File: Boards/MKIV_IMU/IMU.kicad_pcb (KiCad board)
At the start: 2 copper layers, 50.8 x 55.9 mm, 55 parts, among them J1 UF_8_RA, J4 CONN_02X03, Q1 SSM3K333R, Q2 SSM3K333R, U1 CAN_Transceiver, U2 TPS561201, U3 TCR2EF33LM, U4 BMI088, U5 ATMEGA16M1, Y1 Crystal_SMD

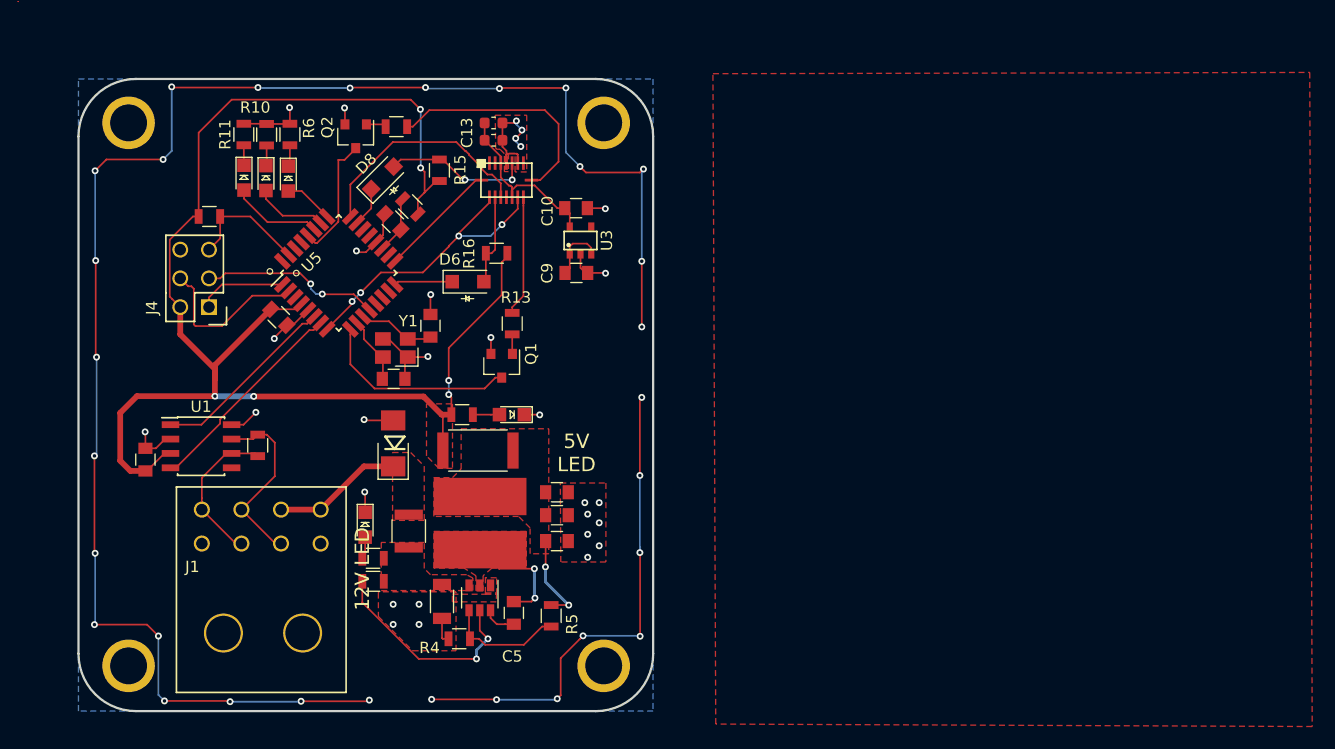
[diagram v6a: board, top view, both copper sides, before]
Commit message: updated fets for layout for new net list
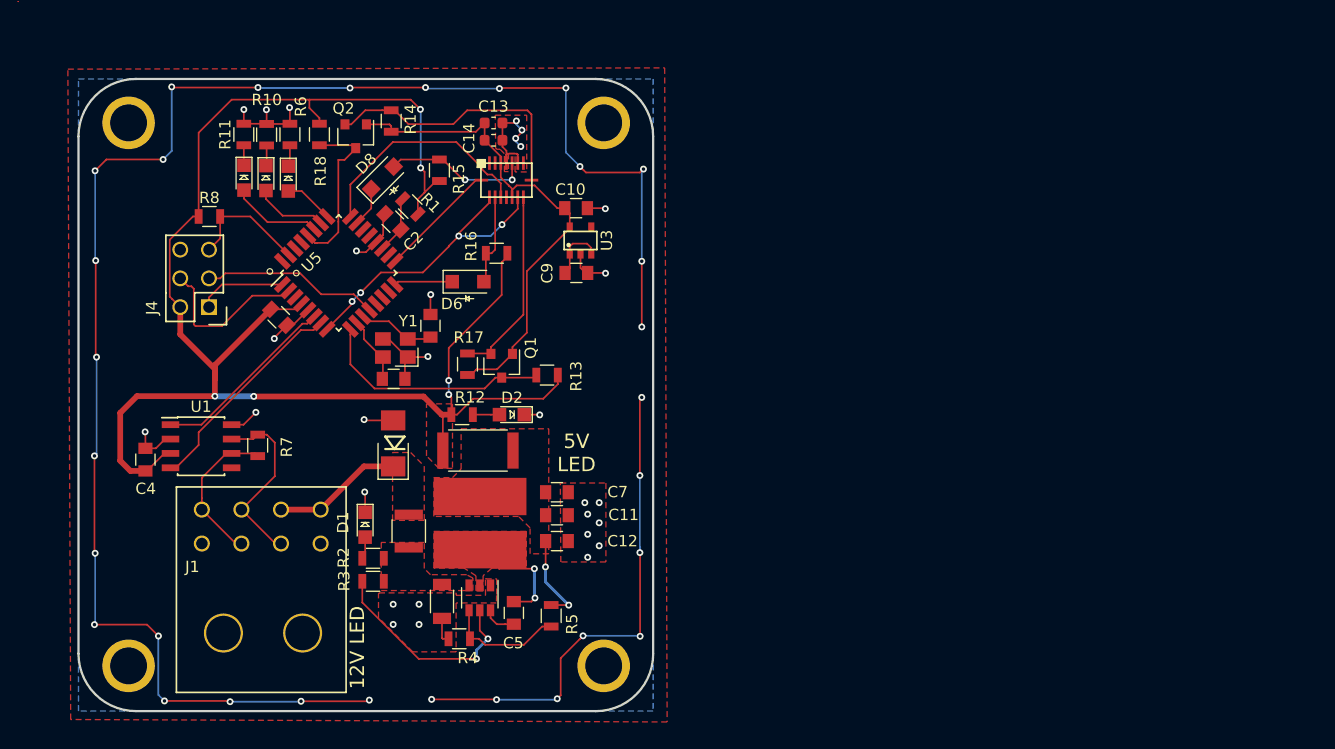
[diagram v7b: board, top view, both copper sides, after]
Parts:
- added R17: R_10K, footprints:R_0805_OEM, F.Cu at (150.0, 96.3)
- added R18: R_10K, footprints:R_0805_OEM, F.Cu at (136.9, 76.0)
- moved G*** 60.5 mm to (144.4, 106.9)
- moved R13 5.49 mm to (157.0, 97.3), turned to 180 degrees
- moved R14 0.68 mm to (143.2, 74.8), turned to 270 degrees
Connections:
- Q1 pad 1: Net-(Q1-Pad1) -> /3.3V
- Q1 pad 2: GND -> Net-(Q1-Pad2)
- Q2 pad 1: Net-(Q2-Pad1) -> /3.3V
- Q2 pad 2: GND -> Net-(Q2-Pad2)
- R13 pad 1: Net-(Q1-Pad1) -> VCC
- R13 pad 2: Net-(R13-Pad2) -> /MOSI2
- R14 pad 1: Net-(Q2-Pad1) -> Net-(Q2-Pad2)
- R14 pad 2: Net-(R14-Pad2) -> /3.3V
- U4 pad 8: Net-(R14-Pad2) -> Net-(Q2-Pad2)
- U4 pad 9: Net-(R13-Pad2) -> Net-(Q1-Pad2)
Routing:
- net /3.3V: track 16.7 -> 44.9 mm
- net Net-(Q2-Pad2): track 0.00 -> 24.0 mm
- net Net-(R14-Pad2): track 20.9 -> 0.00 mm
- net Net-(Q1-Pad2): track 0.00 -> 17.1 mm
- net VCC: track 130.6 -> 144.4 mm
- net Net-(R13-Pad2): track 10.6 -> 0.00 mm
- net /SCK2: track 11.2 -> 15.2 mm
- net /MOSI2: track 17.8 -> 20.9 mm
- net Net-(Q1-Pad1): track 1.73 -> 0.00 mm
- net Net-(Q2-Pad1): track 1.50 -> 0.00 mm
- net /SCK: track 16.0 -> 15.7 mm, vias 2 -> 0
- added copper zone on F.Cu, net VCC
- removed copper zone on F.Cu, net (none)
